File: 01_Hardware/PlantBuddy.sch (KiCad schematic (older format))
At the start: 37 parts, among them J101 J-Link SWD, J102 NFC Antenna, J2 Conn_I2C_SDA, J3 Conn_I2C_SCL, Q101 AO3401A, U101 nRF52832-QFxx, U102 LTR-303ALS-01, U6 SHTC3, Y1 32MHz, Y2 32kHz

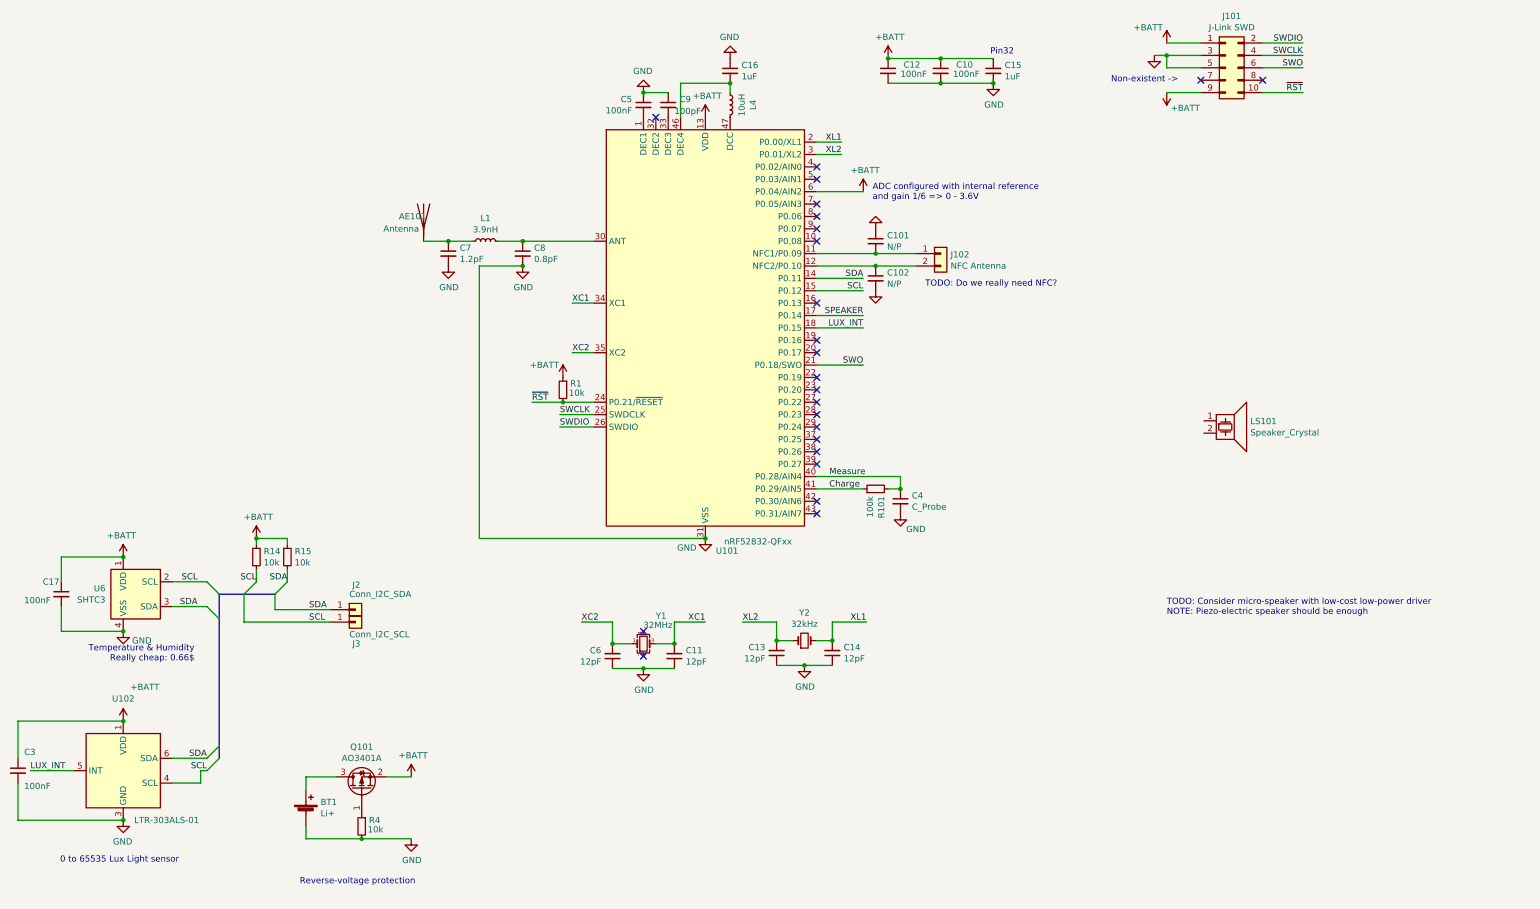
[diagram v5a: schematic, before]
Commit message: Switched to 0603 and re-did layout.
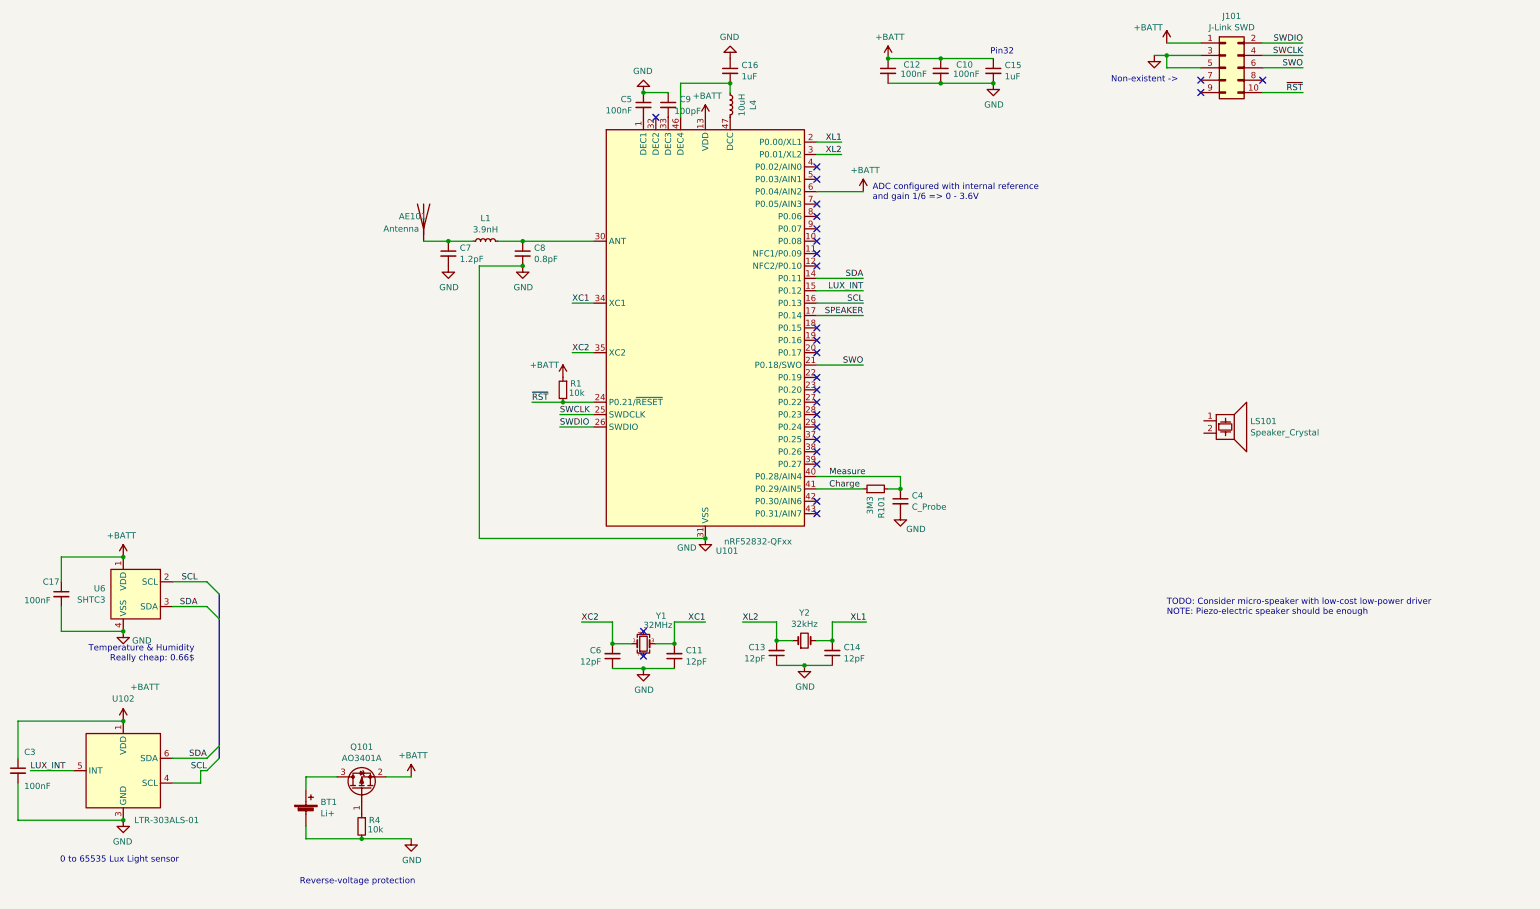
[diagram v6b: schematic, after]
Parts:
- removed C101, C102: N/P, Capacitor_SMD:C_0402_1005Metric, symbol PlantBuddy-rescue:C_Small-Device
- removed J102: NFC Antenna, Connector_PinHeader_2.54mm:PinHeader_1x02_P2.54mm_Vertical, symbol Connector_Generic:Conn_01x02
- removed J2: Conn_I2C_SDA, TestPoint:TestPoint_Pad_D1.0mm, symbol PlantBuddy-rescue:Conn_01x01-Connector_Generic
- removed J3: Conn_I2C_SCL, TestPoint:TestPoint_Pad_D1.0mm, symbol PlantBuddy-rescue:Conn_01x01-Connector_Generic
- removed R14, R15: 10k, Resistor_SMD:R_0402_1005Metric, symbol PlantBuddy-rescue:R_Small-Device
- C10, C11, C12, C13, C14, C15, C16, C17, C3, C5, C6: footprint Capacitor_SMD:C_0402_1005Metric -> Capacitor_SMD:C_0603_1608Metric
- R1, R4: footprint Resistor_SMD:R_0402_1005Metric -> Resistor_SMD:R_0603_1608Metric
- R101: value 100k -> 3M3; footprint Resistor_SMD:R_0402_1005Metric -> Resistor_SMD:R_0603_1608Metric
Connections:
- net +BATT: no longer J101.9 (Pin_9)
- net LUX_INT: now also U101.15 (P0.12); no longer U101.18 (P0.15)
- net SCL: now also U101.16 (P0.13); no longer U101.15 (P0.12)
- no-connect marks 24 -> 27
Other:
- note removed: "TODO: Do we really need NFC?"

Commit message: Done with latest HW revision. To be ordered with Aisler.
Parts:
- LS101: footprint (none) -> Connector_PinHeader_2.54mm:PinHeader_1x02_P2.54mm_Vertical
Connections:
- net at U101.4 (P0.02/AIN0): now also LS101.1
- net at U101.5 (P0.03/AIN1): now also LS101.2
- no-connect marks 27 -> 25
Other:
- note removed: "TODO: Consider micro-speaker with low-cost low-power driver\nNOTE: Piezo-electric speaker should be enough"
- moved on the sheet: LS101
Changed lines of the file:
@@
 	-1   0    0    -1
 $EndComp
-Text Notes 7450 2150 0    50   ~ 0
+Text Notes 7975 2400 0    50   ~ 0
 ADC configured with internal reference\nand gain 1/6 => 0 - 3.6V
-Wire Wire Line
-	7375 2075 7000 2075
 $Comp
 L PlantBuddy-rescue:+BATT-power #PWR0119
 U 1 1 6045E4C9
-P 7375 2075
-F 0 "#PWR0119" H 7375 1925 50  0001 C CNN
-F 1 "+BATT" H 7390 2248 50  0000 C CNN
-F 2 "" H 7375 2075 50  0001 C CNN
-F 3 "" H 7375 2075 50  0001 C CNN
-	1    7375 2075
+P 8225 2175
+F 0 "#PWR0119" H 8225 2025 50  0001 C CNN
+F 1 "+BATT" H 8240 2348 50  0000 C CNN
+F 2 "" H 8225 2175 50  0001 C CNN
+F 3 "" H 8225 2175 50  0001 C CNN
+	1    8225 2175
 	1    0    0    -1
 $EndComp
@@
 NoConn ~ 7000 2275
 NoConn ~ 7000 2175
-NoConn ~ 7000 1975
-NoConn ~ 7000 1875
 Wire Wire Line
 	9825 975  9825 1075
@@
 Wire Wire Line
 	2025 6850 1800 6850
-Text Notes 9825 5500 0    50   ~ 0
-TODO: Consider micro-speaker with low-cost low-power driver\nNOTE: Piezo-electric speaker should be enough
 $Comp
 L PlantBuddy-rescue:Battery_Cell-Device BT1
@@
 L Device:Speaker_Crystal LS101
 U 1 1 6138F133
-P 10325 3925
-F 0 "LS101" H 10500 3921 50  0000 L CNN
-F 1 "Speaker_Crystal" H 10500 3830 50  0000 L CNN
-F 2 "" H 10290 3875 50  0001 C CNN
-F 3 "~" H 10290 3875 50  0001 C CNN
-	1    10325 3925
+P 7300 1875
+F 0 "LS101" H 7475 1871 50  0000 L CNN
+F 1 "Speaker_Crystal" H 7475 1780 50  0000 L CNN
+F 2 "Connector_PinHeader_2.54mm:PinHeader_1x02_P2.54mm_Vertical" H 7265 1825 50  0001 C CNN
+F 3 "~" H 7265 1825 50  0001 C CNN
+	1    7300 1875
 	1    0    0    -1
 $EndComp
@@
 NoConn ~ 7000 2575
 NoConn ~ 7000 2675
+Wire Wire Line
+	7100 1875 7000 1875
+Wire Wire Line
+	7100 1975 7000 1975
+Wire Wire Line
+	7000 2075 7300 2075
+Wire Wire Line
+	7300 2075 7300 2175
+Wire Wire Line
+	7300 2175 8225 2175
 Wire Bus Line
 	2175 5325 2175 6650

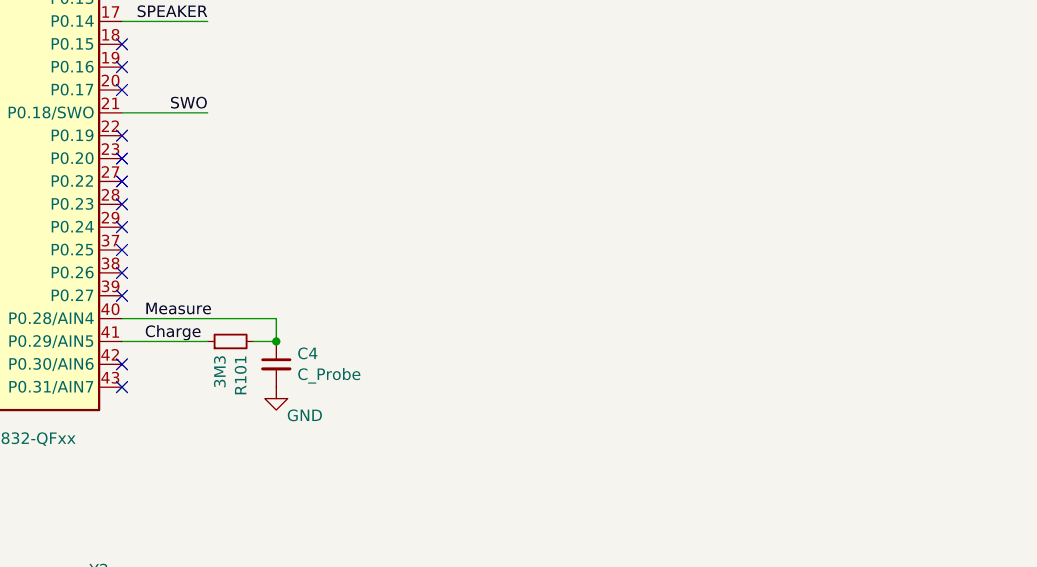
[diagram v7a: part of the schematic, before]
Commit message: Slight schematic TODO added
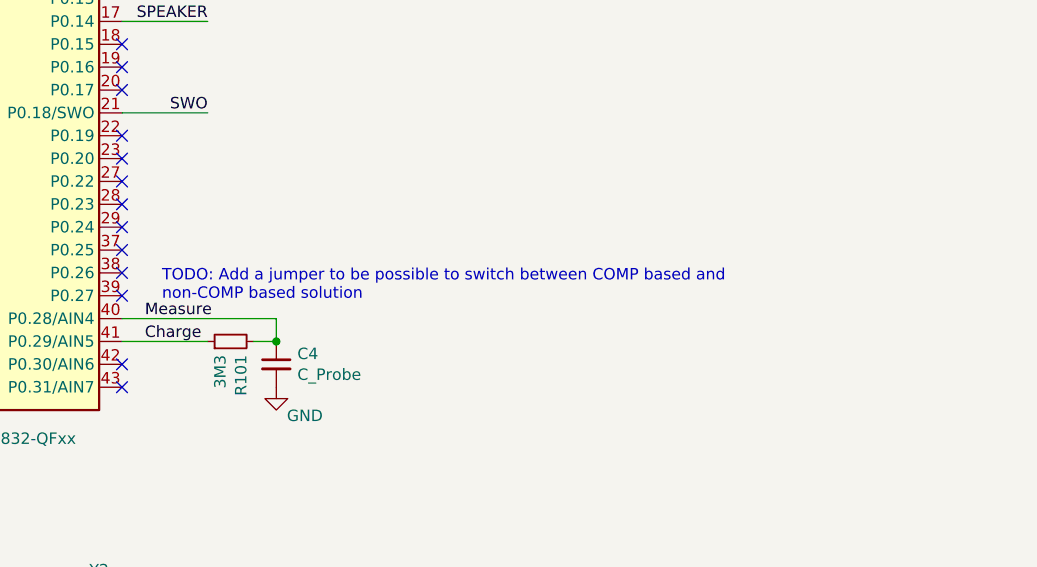
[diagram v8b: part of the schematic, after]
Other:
- note added: "TODO: Add a jumper to be possible to switch between COMP based and\nnon-COMP based solution"
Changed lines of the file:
@@
 Wire Wire Line
 	7300 2175 8225 2175
+Text Notes 7175 4300 0    50   ~ 0
+TODO: Add a jumper to be possible to switch between COMP based and\nnon-COMP based solution
 Wire Bus Line
 	2175 5325 2175 6650
